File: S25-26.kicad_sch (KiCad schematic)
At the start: 41 parts, among them IC1 CMV4000-3E5M0PN, IC2 MXL86110I-AQB-R, J1 DC_IN_PADS, J2 Conn_01x04_Pin, J3 Conn_01x02_Pin, J4 RJ45_RB1-125B8G1A

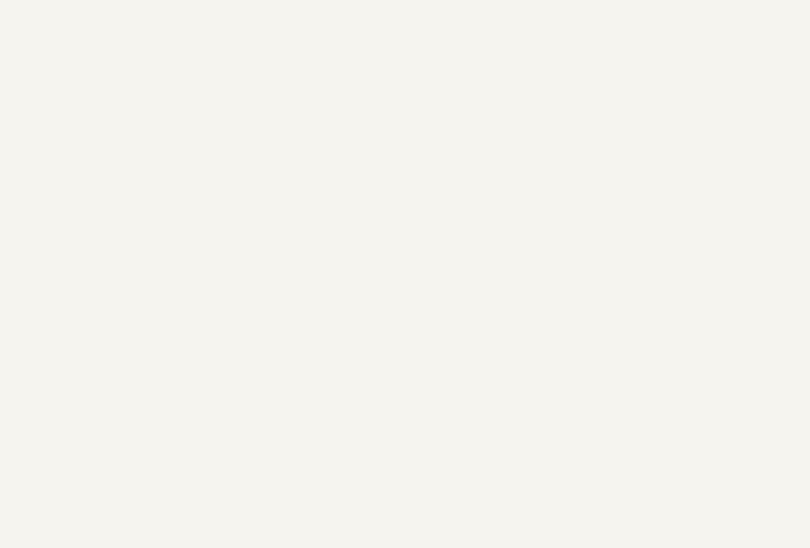
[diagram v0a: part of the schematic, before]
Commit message: Watch Out: David's Mounting Holes
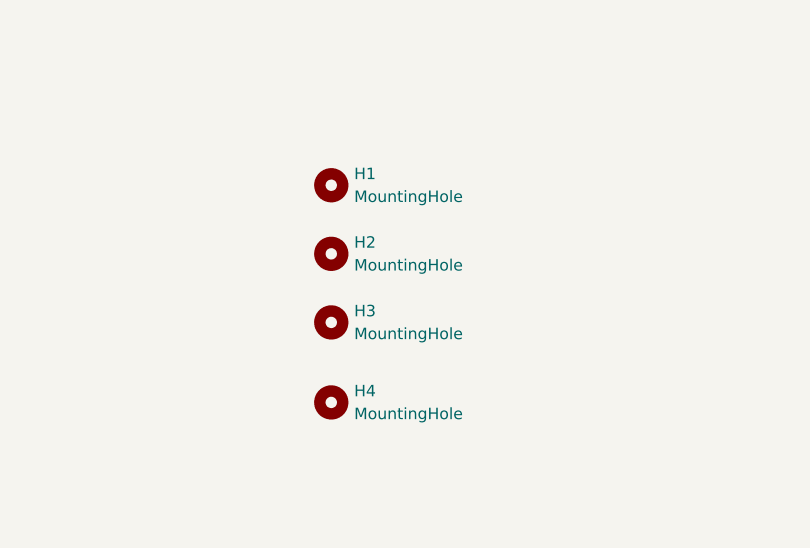
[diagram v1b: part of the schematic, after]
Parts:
- added H1, H2, H3, H4: MountingHole, MountingHole:MountingHole_2.7mm, symbol Mechanical:MountingHole

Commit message: Lots of small changes
Some power and ground planes need to be looked at
All parts need to be reexamined before ordering
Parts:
- added J5: Conn_01x04_Pin, Connector_PinHeader_2.54mm:PinHeader_1x04_P2.54mm_Vertical, symbol Connector:Conn_01x04_Pin
- J2: value Conn_01x04_Pin -> Conn_01x06_Pin; footprint Connector_PinHeader_2.54mm:PinHeader_1x04_P2.54mm_Vertical -> Connector_PinHeader_2.54mm:PinHeader_1x06_P2.54mm_Vertical; symbol Connector:Conn_01x04_Pin -> Connector:Conn_01x06_Pin; now in the parts list
- J3: value Conn_01x02_Pin -> Conn_01x04_Pin; footprint Connector:JWT_A3963_1x02_P3.96mm_Vertical -> Connector_PinHeader_2.54mm:PinHeader_1x04_P2.54mm_Vertical; symbol Connector:Conn_01x02_Pin -> Connector:Conn_01x04_Pin; now in the parts list
- J4: value RJ45_RB1-125B8G1A -> RJ45_JXD1-0001NL; Digikey Part Number (none) -> 553-3266-ND; Digikey Price/Stock (none) -> https://www.digikey.com/en/products/detail/pulse-electronic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
- RLVDS1: Mouser Part Number 71-CRCW0603100RFKEAH -> 667-ERJ-P03F1000V; Mouser Price/Stock https://www.mouser.com/ProductDetail/Vishay-Dale/CRCW060310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 -> https://www.mouser.com/ProductDetail/Panasonic/ERJ-P03F1000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; Power Rating 0.33W -> 0.2W
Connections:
- net GND: now also J2.6 (Pin_6)
- net JTAG_SWCLK renamed Processing/SWJ_SWCLK_TCLK
- net JTAG_SWDIO renamed Processing/SWJ_SWDIO_TMS
- net JTAG_SWO renamed Processing/SWJ_SWO_TDO
- net JTAG_TDI renamed Processing/SWJ_SWDOE_TDI
- net SCB3_RX renamed Processing/SCB3_RX (P17.1)
- net SCB3_TX renamed Processing/SCB3_CTS
- new net Processing/SCB3_RTS: J3.4 (Pin_4)
- new net Processing/SCB3_TX (P17.2): J3.3 (Pin_3)
- new net Processing/SCB8_CTS: J5.2 (Pin_2)
- new net Processing/SCB8_RTS: J5.4 (Pin_4)
- new net Processing/SCB8_RX: J5.1 (Pin_1)
- new net Processing/SCB8_TX: J5.3 (Pin_3)
- new net Processing/SWJ_TRSTN: J2.5 (Pin_5)
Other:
- sheet Processing ports: added SCB3_CTS, SCB3_RTS, SCB8_CTS, SCB8_RTS, SCB8_RX, SCB8_TX, SWJ_SWCLK_TCLK, SWJ_SWDIO_TMS, SWJ_SWDOE_TDI, SWJ_SWO_TDO, SWJ_TRSTN; removed JTAG_SWCLK (P23.5), JTAG_SWDIO (P23.6), JTAG_SWO (P23.4), JTAG_TDI (P23.7)

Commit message: See previous push
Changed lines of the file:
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@@
 	(wire
 		(pts
-			(xy 92.71 34.29) (xy 95.25 34.29)
+			(xy 92.71 34.29) (xy 96.52 34.29)
 		)
 		(stroke
@@
 	(global_label "+2V1"
 		(shape input)
-		(at 95.25 34.29 0)
+		(at 96.52 34.29 0)
 		(fields_autoplaced yes)
 		(effects
@@
 		)
 		(property "Intersheetrefs" "${INTERSHEET_REFS}"
-			(at 103.3152 34.29 0)
+			(at 104.5852 34.29 0)
 			(effects
 				(font

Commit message: Almost done
Taking a break and making a push. Known things to do:
Add pull-up resistors to ETH MDIO, ETH MDC, and XRESL.
Source a 100uF capacitor for primary regulator.
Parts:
- added R12: 60, Resistor_SMD:R_1206_3216Metric, symbol Device:R
- added R13: 56, Resistor_SMD:R_1206_3216Metric, symbol Device:R
- C1, C10, C11, C12, C13, C14, C15, C16, C17, C18, C19, C2, C20, C3, C4, C5, C6, C7, C8, C9: footprint Capacitor_SMD:C_0603_1608Metric -> Capacitor_SMD:C_1206_3216Metric; Mouser Part Number 81-GCM188R71C104KA7J -> 581-12065C104J4Z2A; Mouser Price/Stock https://www.mouser.com/ProductDetail/Murata-Electronics/GCM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 -> https://www.mouser.com/ProductDetail/KYOCERA-AVX/12065C104J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; Package Size (none) -> 1206; Tolerance 10% -> 5%; Voltage Rating 16V -> 50V
- R1, R2: Mouser Part Number 71-CRCW06031K00FKED -> 71-RCA12061K00FKEA; Mouser Price/Stock https://www.mouser.com/ProductDetail/Vishay-Dale/CRCW06031K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 -> https://www.mouser.com/ProductDetail/Vishay-Draloric/RCA120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; Package Size (none) -> 1206; Power Rating 0.25W -> 250mW
- R3: footprint Resistor_SMD:R_0603_1608Metric -> Resistor_SMD:R_1206_3216Metric; Mouser Part Number 71-CRCW06032K49FKEAH -> 603-RC1206FR-102K49L; Mouser Price/Stock https://www.mouser.com/ProductDetail/Vishay-Dale/CRCW06032K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 -> https://www.mouser.com/ProductDetail/YAGEO/RC1206FR-102K49L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; Package Size (none) -> 1206; Power Rating 0.33W -> 250mW
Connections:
- net GND: now also C19.1, C20.1; no longer C19.2, C20.2
- net PHY_LED0: now also R12.1; no longer IC2.32 (GPHY_LED0/CFG_EXT), J4.L3
- net PHY_LED1: now also J4.L3, R13.1; no longer IC2.33 (GPHY_LED1/CFG_LDO0)
- net at IC1.D11 (VREF): now also C19.2; no longer C19.1
- net at IC1.D12 (REF_ADC): now also C20.2; no longer C20.1
- new net: IC2.32 (GPHY_LED0/CFG_EXT), R12.2
- new net: IC2.33 (GPHY_LED1/CFG_LDO0), R13.2

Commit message: See previous push
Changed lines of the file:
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@@
 	(wire
 		(pts
-			(xy 92.71 34.29) (xy 96.52 34.29)
+			(xy 92.71 34.29) (xy 95.25 34.29)
 		)
 		(stroke
@@
 	(global_label "+2V1"
 		(shape input)
-		(at 96.52 34.29 0)
+		(at 95.25 34.29 0)
 		(fields_autoplaced yes)
 		(effects
@@
 		)
 		(property "Intersheetrefs" "${INTERSHEET_REFS}"
-			(at 104.5852 34.29 0)
+			(at 103.3152 34.29 0)
 			(effects
 				(font

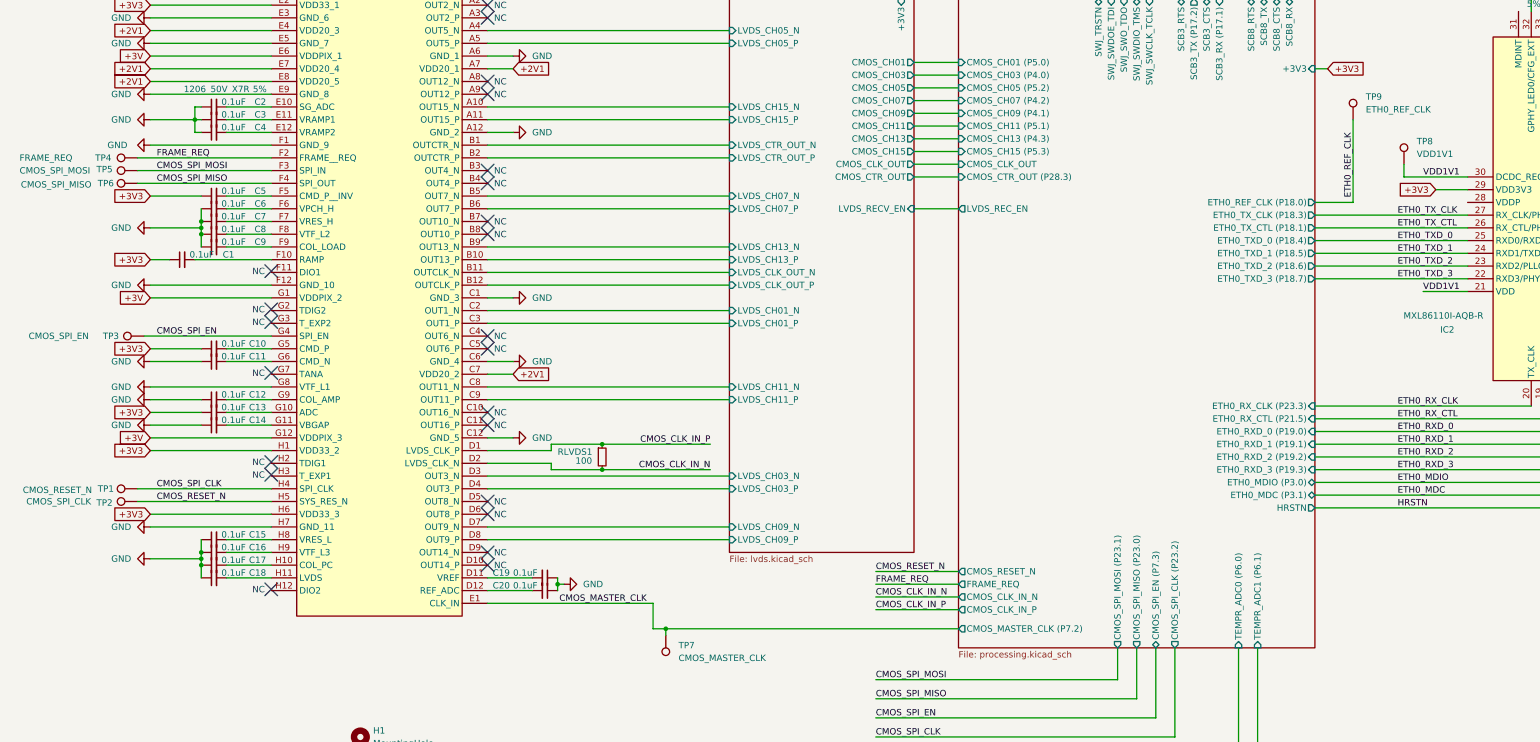
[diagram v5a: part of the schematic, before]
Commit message: Labeled test pads; marked tantalums with lines for cathode; found suitable tantalum for 100 uF
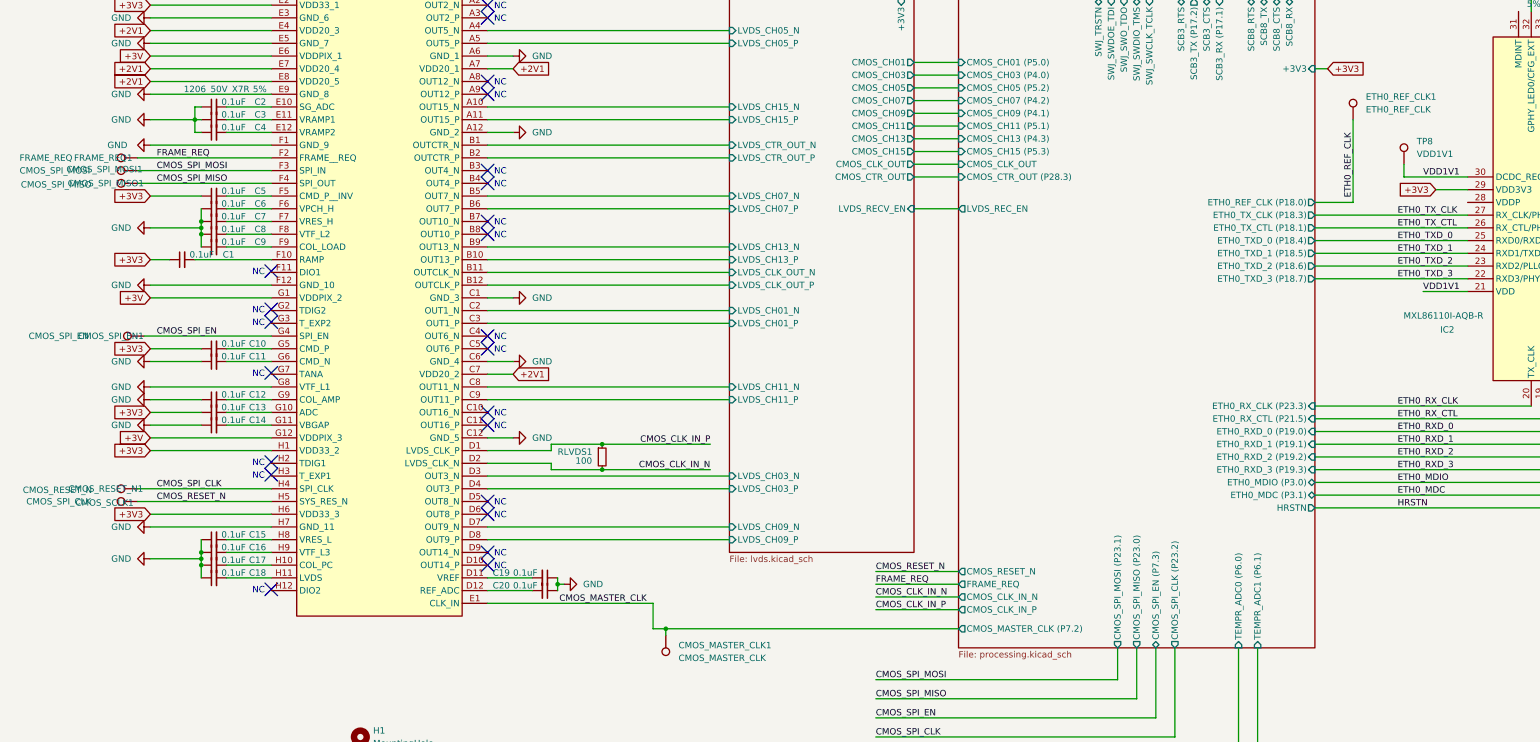
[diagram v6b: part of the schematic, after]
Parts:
- IC1: Arrow Part Number (none) -> CMV4000-3E5M0PN; Arrow Price/Stock (none) -> https://www.arrow.com/en/products/cmv4000-3e5m0pn/ams-ag?re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
- IC2: footprint QFN40P500X500X95-41N-D -> SamacSys_Parts:QFN40P500X500X95-41N-D
- TR1, TR2: footprint RESC3016X65N -> SamacSys_Parts:RESC3016X65N
- renumbered TP7 to CMOS_MASTER_CLK1, TP1 to CMOS_RESET_N1, TP2 to CMOS_SCLK1, TP3 to CMOS_SPI_EN1, TP6 to CMOS_SPI_MISO1, TP5 to CMOS_SPI_MOSI1, TP9 to ETH0_REF_CLK1, TP4 to FRAME_REQ1
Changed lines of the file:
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@@
 			)
 		)
-		(property "Footprint" "QFN40P500X500X95-41N-D"
+		(property "Footprint" "SamacSys_Parts:QFN40P500X500X95-41N-D"
 			(at 306.07 185.09 0)
 			(effects
@@
 		(on_board yes)
 		(dnp no)
-		(property "Reference" "TP4"
+		(property "Reference" "FRAME_REQ1"
 			(at 29.972 111.76 90)
 			(effects
@@
 			(project "S25-26"
 				(path "/6f4563ef-8a79-4567-b913-33c6dfb42b56"
-					(reference "TP4")
+					(reference "FRAME_REQ1")
 					(unit 1)
 				)
@@
 		(dnp no)
 		(fields_autoplaced yes)
-		(property "Reference" "TP9"
+		(property "Reference" "ETH0_REF_CLK1"
 			(at 281.94 99.5679 0)
 			(effects
@@
 			(project "S25-26"
 				(path "/6f4563ef-8a79-4567-b913-33c6dfb42b56"
-					(reference "TP9")
+					(reference "ETH0_REF_CLK1")
 					(unit 1)
 				)
@@
 			)
 		)
+		(property "Arrow Part Number" "CMV4000-3E5M0PN"
+			(at 106.68 81.28 0)
+			(effects
+				(font
+					(size 1.27 1.27)
+				)
+				(hide yes)
+			)
+		)
+		(property "Arrow Price/Stock" "https://www.arrow.com/en/products/cmv4000-3e5m0pn/ams-ag?region=nac"
+			(at 106.68 81.28 0)
+			(effects
+				(font
+					(size 1.27 1.27)
+				)
+				(hide yes)
+			)
+		)
 		(pin "D1"
 		)
@@
 		(on_board yes)
 		(dnp no)
-		(property "Reference" "TP1"
+		(property "Reference" "CMOS_RESET_N1"
 			(at 30.48 177.8 90)
 			(effects
@@
 			(project ""
 				(path "/6f4563ef-8a79-4567-b913-33c6dfb42b56"
-					(reference "TP1")
+					(reference "CMOS_RESET_N1")
 					(unit 1)
 				)
@@
 		(on_board yes)
 		(dnp no)
-		(property "Reference" "TP3"
+		(property "Reference" "CMOS_SPI_EN1"
 			(at 31.496 147.32 90)
 			(effects
@@
 			(project "S25-26"
 				(path "/6f4563ef-8a79-4567-b913-33c6dfb42b56"
-					(reference "TP3")
+					(reference "CMOS_SPI_EN1")
 					(unit 1)
 				)
@@
 		(on_board yes)
 		(dnp no)
-		(fields_autoplaced yes)
-		(property "Reference" "TP7"
+		(property "Reference" "CMOS_MASTER_CLK1"
 			(at 144.78 209.0419 0)
 			(effects
@@
 			(project "S25-26"
 				(path "/6f4563ef-8a79-4567-b913-33c6dfb42b56"
-					(reference "TP7")
+					(reference "CMOS_MASTER_CLK1")
 					(unit 1)
 				)
@@
 			)
 		)
-		(property "Footprint" "RESC3016X65N"
+		(property "Footprint" "SamacSys_Parts:RESC3016X65N"
 			(at 287.02 341.3 0)
 			(effects
@@
 		(on_board yes)
 		(dnp no)
-		(property "Reference" "TP5"
+		(property "Reference" "CMOS_SPI_MOSI1"
 			(at 30.226 114.046 90)
 			(effects
@@
 			(project "S25-26"
 				(path "/6f4563ef-8a79-4567-b913-33c6dfb42b56"
-					(reference "TP5")
+					(reference "CMOS_SPI_MOSI1")
 					(unit 1)
 				)
@@
 			)
 		)
-		(property "Footprint" "RESC3016X65N"
+		(property "Footprint" "SamacSys_Parts:RESC3016X65N"
 			(at 226.06 341.3 0)
 			(effects
@@
 		(on_board yes)
 		(dnp no)
-		(property "Reference" "TP6"
+		(property "Reference" "CMOS_SPI_MISO1"
 			(at 30.48 116.84 90)
 			(effects
@@
 			(project "S25-26"
 				(path "/6f4563ef-8a79-4567-b913-33c6dfb42b56"
-					(reference "TP6")
+					(reference "CMOS_SPI_MISO1")
 					(unit 1)
 				)
@@
 		(on_board yes)
 		(dnp no)
-		(property "Reference" "TP2"
+		(property "Reference" "CMOS_SCLK1"
 			(at 30.226 180.594 90)
 			(effects
@@
 			(project "S25-26"
 				(path "/6f4563ef-8a79-4567-b913-33c6dfb42b56"
-					(reference "TP2")
+					(reference "CMOS_SCLK1")
 					(unit 1)
 				)
@@
 		(on_board yes)
 		(dnp no)
-		(fields_autoplaced yes)
 		(property "Reference" "TP8"
 			(at 292.1 108.4579 0)

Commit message: Beginning of V3
Long way to go
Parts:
- removed IC2: MXL86110I-AQB-R, SamacSys_Parts:QFN40P500X500X95-41N-D, symbol SamacSys_Parts:MXL86110C-AQB-R
- removed R3: 2.49k, Resistor_SMD:R_1206_3216Metric, symbol Device:R_Small
- removed TP8: VDD1V1, TestPoint:TestPoint_Pad_2.0x2.0mm, symbol Connector:TestPoint
- added IC11: DP83867IRPAPT, QFP50P1200X1200X120-65N, symbol SamacSys_Parts:DP83867IRPAPT
- added R17, R18, R19: 10k, Resistor_SMD:R_1206_3216Metric, symbol Device:R
- IC1: footprint SamacSys_Parts:CMV40003E5M0PN -> CustomFootprintLibrary:CMV40003E5M0PN_Socket
- J2: footprint Connector_PinHeader_2.54mm:PinHeader_1x06_P2.54mm_Vertical -> Connector_PinHeader_1.27mm:PinHeader_2x05_P1.27mm_Vertical_SMD; symbol Connector:Conn_01x06_Pin -> Connector_Generic:Conn_02x05_Odd_Even
- J4: footprint Connector_RJ:RJ45_UDE_RB1-125B8G1A -> CustomFootprintLibrary:RJ45_JXD1-0001NL
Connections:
- net Processing/SWJ_TRSTN is gone; now on net GND: J2.5 (Pin_5)
- net +3V3: now also J2.1 (Pin_1), R17.2, R18.2, R19.2
- net BI_DA_N: now also IC11.3 (TD_M_A)
- net BI_DA_P: now also IC11.2 (TD_P_A)
- net BI_DB_N: now also IC11.6 (TD_M_B)
- net BI_DB_P: now also IC11.5 (TD_P_B)
- net BI_DC_N: now also IC11.11 (TD_M_C)
- net BI_DC_P: now also IC11.10 (TD_P_C)
- net BI_DD_N: now also IC11.14 (TD_M_D)
- net BI_DD_P: now also IC11.13 (TD_P_D)
- net ETH0_MDC: now also IC11.20 (MDC)
- net ETH0_MDIO: now also IC11.21 (MDIO)
- net ETH0_RXD_0: now also IC11.44 (RX_D0)
- net ETH0_RXD_1: now also IC11.45 (RX_D1)
- net ETH0_RXD_2: now also IC11.46 (RX_D2)
- net ETH0_RXD_3: now also IC11.47 (RX_D3)
- net ETH0_RX_CLK: now also IC11.43 (RX_CLK)
- net ETH0_RX_CTL: now also IC11.53 (RX_DV/RX_CTRL)
- net ETH0_TXD_0: now also IC11.38 (TX_D0)
- net ETH0_TXD_1: now also IC11.37 (TX_D1)
- net ETH0_TXD_2: now also IC11.36 (TX_D2)
- net ETH0_TXD_3: now also IC11.35 (TX_D3)
- net ETH0_TX_CLK: now also IC11.30 (TX_CLK)
- net ETH0_TX_CTL: now also IC11.52 (TX_EN/TX_CTRL)
- net GND: now also J2.3 (Pin_3), J2.7 (Pin_7), J2.9 (Pin_9); no longer J2.6 (Pin_6)
- net Processing/SWJ_SWCLK_TCLK: now also J2.4 (Pin_4), R18.1; no longer J2.1 (Pin_1)
- net Processing/SWJ_SWDIO_TMS: now also R19.1
- net Processing/SWJ_SWDOE_TDI: now also J2.8 (Pin_8), R17.1; no longer J2.4 (Pin_4)
- net Processing/SWJ_SWO_TDO: now also J2.6 (Pin_6); no longer J2.3 (Pin_3)
- new net Processing/XRES: J2.10 (Pin_10)
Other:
- sheet Processing ports: added XRES; removed SWJ_TRSTN
- moved on the sheet: ETH0_REF_CLK1, J4, R12, R13

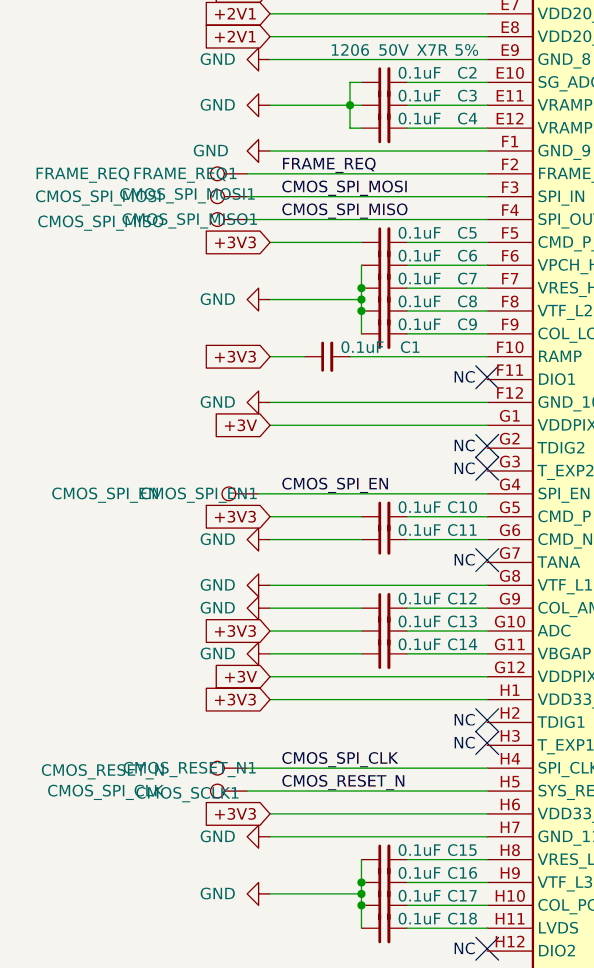
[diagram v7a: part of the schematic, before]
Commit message: Excluded TPs from BOM
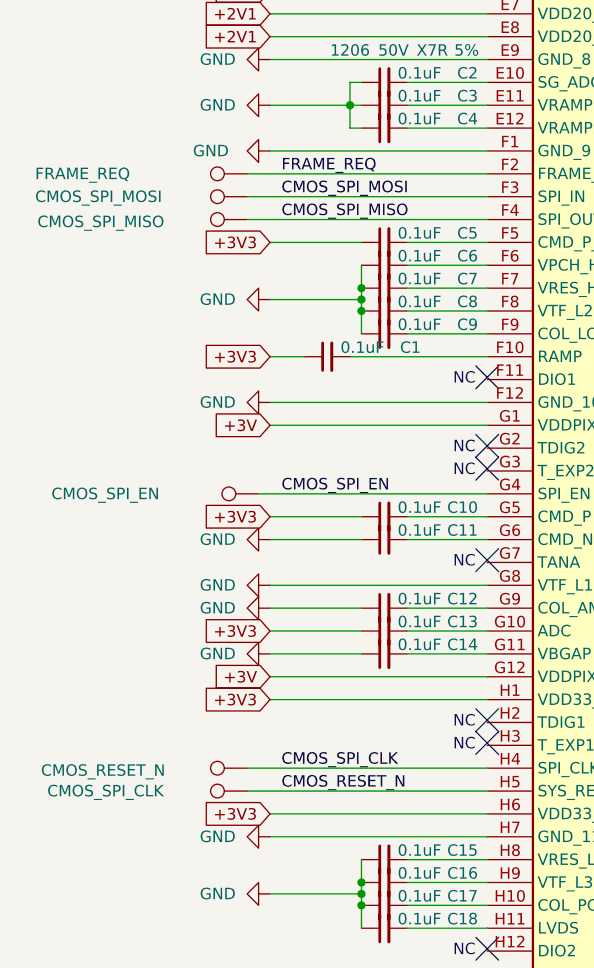
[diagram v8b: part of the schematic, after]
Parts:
- CMOS_MASTER_CLK1, CMOS_RESET_N1, CMOS_SCLK1, CMOS_SPI_EN1, CMOS_SPI_MISO1, CMOS_SPI_MOSI1, ETH0_REF_CLK1, FRAME_REQ1: now left out of the parts list
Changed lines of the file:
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@@
 		(unit 1)
 		(exclude_from_sim no)
-		(in_bom yes)
+		(in_bom no)
 		(on_board yes)
 		(dnp no)
 		(property "Reference" "FRAME_REQ1"
-			(at 29.972 111.76 90)
+			(at 26.67 111.76 90)
 			(effects
 				(font
 					(size 1.27 1.27)
 				)
+				(hide yes)
 			)
 		)
@@
 		(unit 1)
 		(exclude_from_sim no)
-		(in_bom yes)
+		(in_bom no)
 		(on_board yes)
 		(dnp no)
@@
 		(unit 1)
 		(exclude_from_sim no)
-		(in_bom yes)
+		(in_bom no)
 		(on_board yes)
 		(dnp no)
@@
 					(size 1.27 1.27)
 				)
+				(hide yes)
 			)
 		)
@@
 		(unit 1)
 		(exclude_from_sim no)
-		(in_bom yes)
+		(in_bom no)
 		(on_board yes)
 		(dnp no)
@@
 					(size 1.27 1.27)
 				)
+				(hide yes)
 			)
 		)
@@
 		(unit 1)
 		(exclude_from_sim no)
-		(in_bom yes)
+		(in_bom no)
 		(on_board yes)
 		(dnp no)
@@
 		(unit 1)
 		(exclude_from_sim no)
-		(in_bom yes)
+		(in_bom no)
 		(on_board yes)
 		(dnp no)
@@
 					(size 1.27 1.27)
 				)
+				(hide yes)
 			)
 		)
@@
 		(unit 1)
 		(exclude_from_sim no)
-		(in_bom yes)
+		(in_bom no)
 		(on_board yes)
 		(dnp no)
@@
 					(size 1.27 1.27)
 				)
+				(hide yes)
 			)
 		)
@@
 		(unit 1)
 		(exclude_from_sim no)
-		(in_bom yes)
+		(in_bom no)
 		(on_board yes)
 		(dnp no)
@@
 					(size 1.27 1.27)
 				)
+				(hide yes)
 			)
 		)
